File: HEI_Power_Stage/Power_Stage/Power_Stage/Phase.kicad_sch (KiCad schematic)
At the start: 44 parts, among them IC1 AHV85111KNHTR, IC4 AHV85111KNHTR, Q1 EPC2304ENGRT, Q2 EPC2304ENGRT, T1 30k, T2 30k

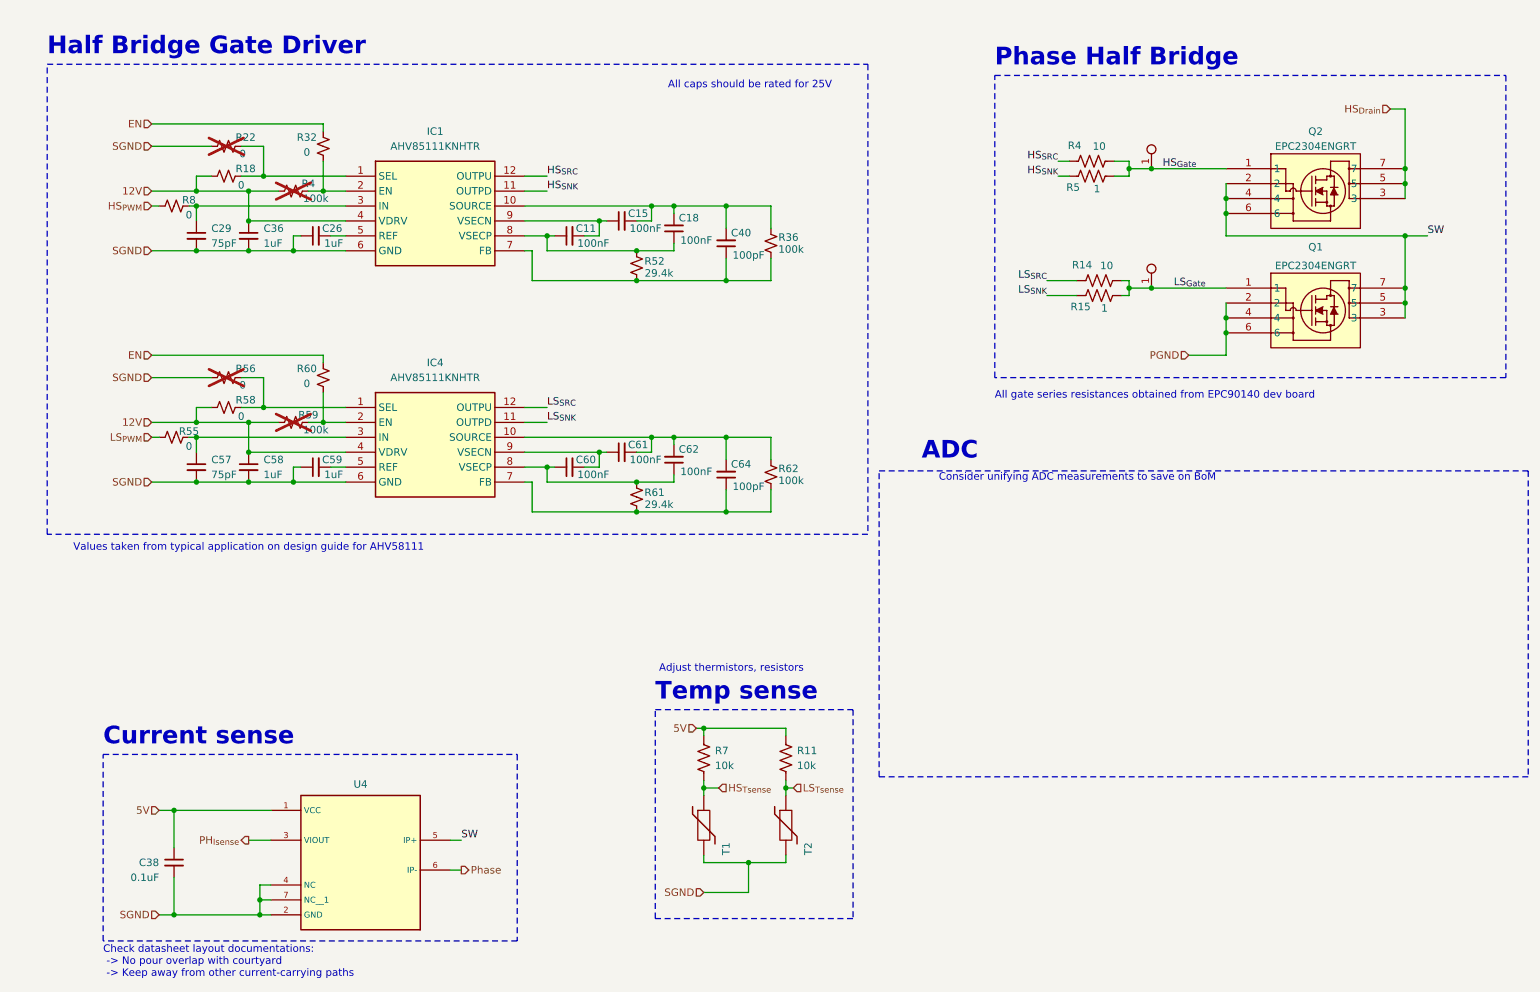
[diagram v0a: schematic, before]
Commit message: new power stage schematic
added iso amp for hv bus sensing
updated connectors
removed isolation page
added notes for new components
need to decide if ADCs go on power or logic board for noise immunity or simpler power stage
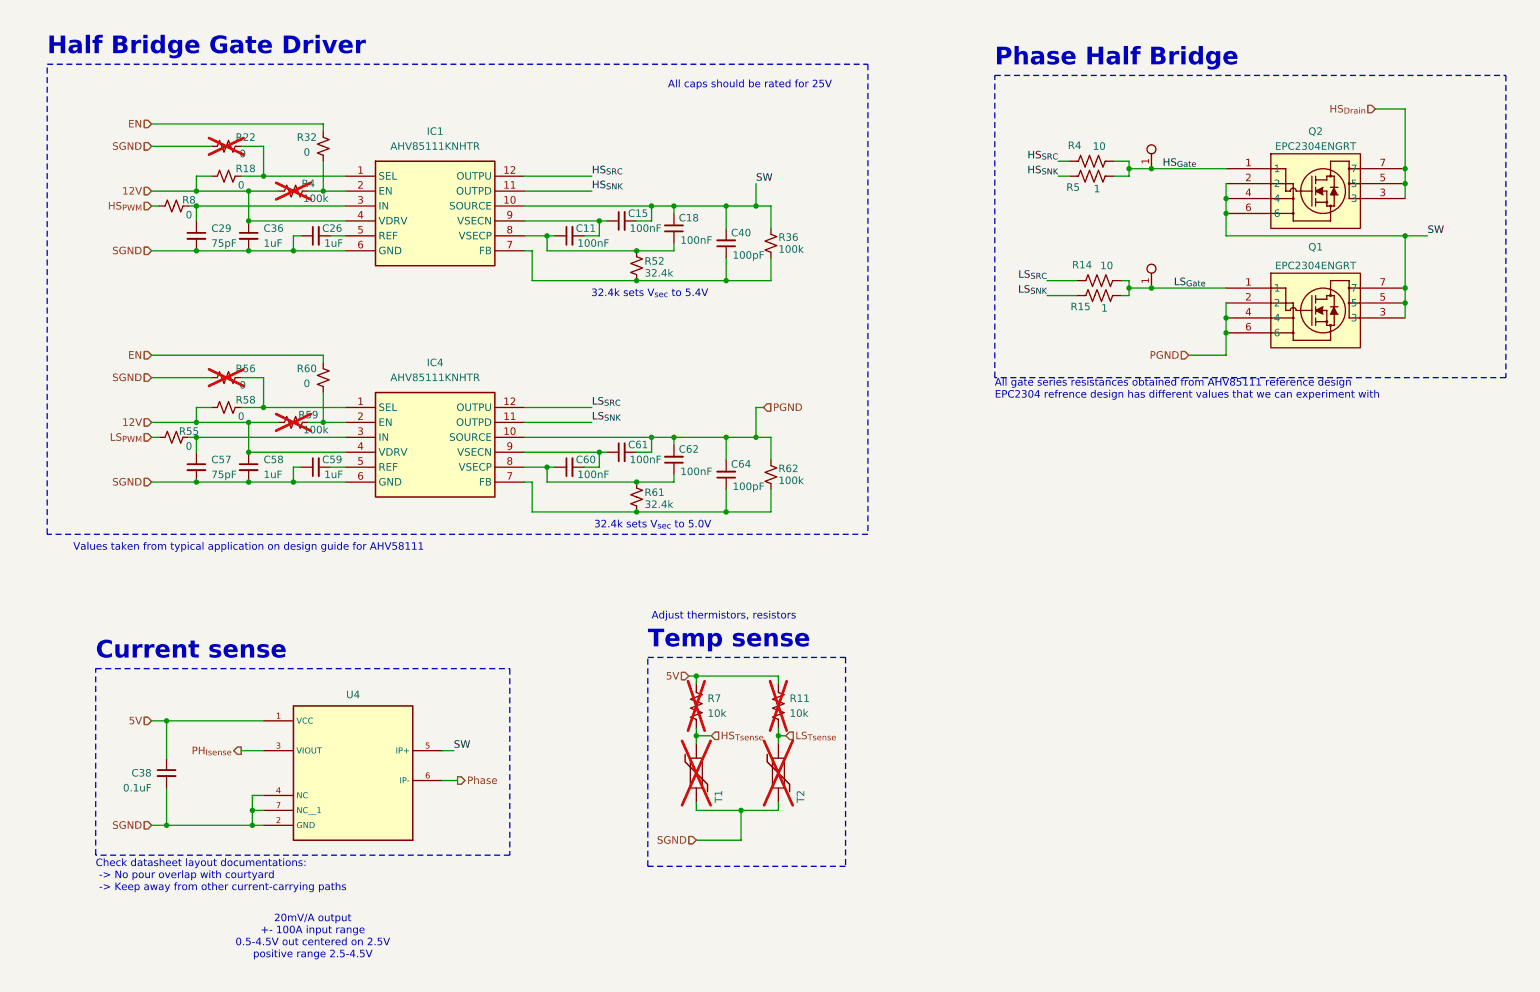
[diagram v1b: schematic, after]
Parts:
- R11, R7, T1, T2: now not fitted
- R52, R61: value 29.4k -> 32.4k
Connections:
- net PGND: now also C61.2, C62.2, C64.2, IC4.10 (SOURCE), R62.1
- net SW: now also C15.2, C18.2, C40.2, IC1.10 (SOURCE), R36.1
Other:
- note added: "20mV/A output +- 100A input range 0.5-4.5V out centered on 2.5V positive range 2.5-4.5V"
- note added: "32.4k sets V_{sec} to 5.0V"
- note added: "32.4k sets V_{sec} to 5.4V"
- note added: "All gate series resistances obtained from AHV85111 reference design EPC2304 refrence design has different values that we can experiment with"
- note removed: "ADC"
- note removed: "All gate series resistances obtained from EPC90140 dev board"
- note removed: "Consider unifying ADC measurements to save on BoM"
- moved on the sheet: C38, U4

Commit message: I think all schematic done
added new mps gate driver, new acs current sense, new differential voltage sense, new 5-5 iso converters.
beginning layout
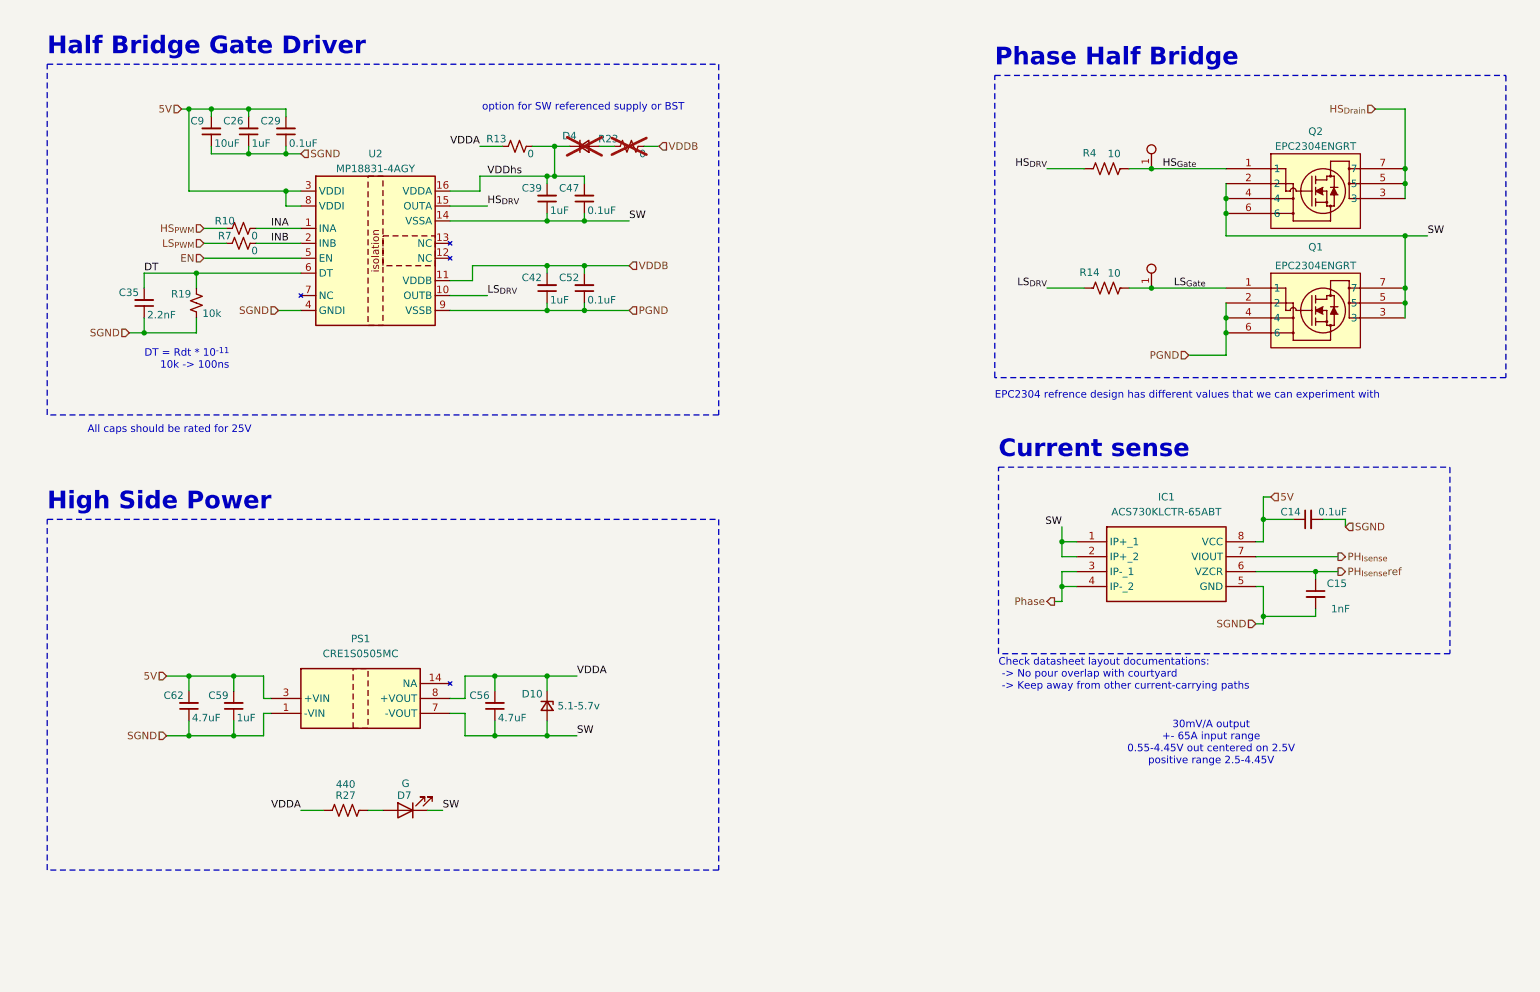
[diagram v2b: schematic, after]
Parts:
- removed C11, C18, C60, C61: 100nF, symbol Device:C_Small
- removed C36, C58: 1uF, symbol Device:C_Small
- removed C38: 0.1uF, Capacitor_SMD:C_0603_1608Metric_Pad1.08x0.95mm_HandSolder, symbol Device:C_Small
- removed C40, C64: 100pF, symbol Device:C_Small
- removed C57: 75pF, symbol Device:C_Small
- removed IC1, IC4: AHV85111KNHTR, AHV85111KNHTR, symbol AHV85111KNHTR:AHV85111KNHTR
- removed R11, R7: 10k, Resistor_SMD:R_0603_1608Metric_Pad0.98x0.95mm_HandSolder, symbol Device:R_US
- removed R15, R5: 1, Resistor_SMD:R_0603_1608Metric_Pad0.98x0.95mm_HandSolder, symbol Device:R_US
- removed R18, R22, R32, R55, R56, R58, R60, R8: 0, symbol Device:R_Small_US
- removed R36, R4, R59, R62: 100k, symbol Device:R_Small_US
- removed R52, R61: 32.4k, symbol Device:R_Small_US
- removed T1, T2: 30k, GTSR_KiCAD_Footprints_SD:2152723803, symbol Device:Thermistor
- removed U4: ~, GTSR_KiCAD_Footprints_SD:XDCR_ACS72981LLRATR-100B5, symbol GTSR_symbol_lib_SD:ACS72981LLRATR-100B5
- added C14, C47, C52: 0.1uF, Capacitor_SMD:C_0603_1608Metric_Pad1.08x0.95mm_HandSolder, symbol Device:C_Small
- added C35: 2.2nF, Capacitor_SMD:C_0603_1608Metric_Pad1.08x0.95mm_HandSolder, symbol Device:C_Small
- added C39, C42: 1uF, Capacitor_SMD:C_0603_1608Metric_Pad1.08x0.95mm_HandSolder, symbol Device:C_Small
- added C56: 4.7uF, Capacitor_SMD:C_0603_1608Metric_Pad1.08x0.95mm_HandSolder, symbol Device:C_Small
- added C9: 10uF, Capacitor_SMD:C_0603_1608Metric_Pad1.08x0.95mm_HandSolder, symbol Device:C_Small
- added D10: 5.1-5.7v, Diode_SMD:D_SOD-128, symbol Device:D_Zener_Small
- added D4: ~, Diode_SMD:D_SOD-523, symbol Device:D_Small
- added D7: G, LED_SMD:LED_0603_1608Metric_Pad1.05x0.95mm_HandSolder, symbol Device:LED
- added IC1: ACS730KLCTR-65ABT, ACS730KLCTR65ABT_KiCad:SOIC127P600X175-8N, symbol ACS730KLCTR-30AB-T:ACS730KLCTR-30AB-T
- added PS1: CRE1S0505MC, CRE1S0505MC_KiCad:CRE1S0505MC, symbol CRE1S0505MC:CRE1S0505MC
- added R10, R13, R7: 0, Resistor_SMD:R_0603_1608Metric_Pad0.98x0.95mm_HandSolder, symbol Device:R_Small_US
- added R19: 10k, Resistor_SMD:R_0603_1608Metric_Pad0.98x0.95mm_HandSolder, symbol Device:R_Small_US
- added R23: 0, LED_SMD:LED_0603_1608Metric_Pad1.05x0.95mm_HandSolder, symbol Device:R_Small_US
- added R27: 440, Resistor_SMD:R_0603_1608Metric_Pad0.98x0.95mm_HandSolder, symbol Device:R_US
- added U2: MP18831-4AGY, Package_SO:SOIC-16W_7.5x10.3mm_P1.27mm, symbol AHV85111KNHTR:MP18831
- C15: value 100nF -> 1nF; footprint (none) -> Capacitor_SMD:C_0603_1608Metric_Pad1.08x0.95mm_HandSolder
- C26, C59: footprint (none) -> Capacitor_SMD:C_0603_1608Metric_Pad1.08x0.95mm_HandSolder
- C29: value 75pF -> 0.1uF; footprint (none) -> Capacitor_SMD:C_0603_1608Metric_Pad1.08x0.95mm_HandSolder
- C62: value 100nF -> 4.7uF; footprint (none) -> Capacitor_SMD:C_0603_1608Metric_Pad1.08x0.95mm_HandSolder
- Q1, Q2: footprint GTSR_KiCAD_Footprints:EPC2304_ECC -> GTSR:EPC2304_ECC
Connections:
- net 5V: now also C26.2, C29.2, C59.2, C62.2, C14.1, C9.2, IC1.8 (VCC), PS1.3 (+VIN), U2.3 (VDDI), U2.8 (VDDI)
- net EN: now also U2.5 (EN)
- net HS_{PWM}: now also R10.1
- net LS_{PWM}: now also R7.1
- net PGND: now also C42.1, C52.1, U2.9 (VSSB); no longer C62.2
- net PH_{Isense}: now also IC1.7 (VIOUT)
- net Phase: now also IC1.3 (IP-_1), IC1.4 (IP-_2)
- net SGND: now also C15.2, C29.1, C62.1, C14.2, C35.1, C9.1, IC1.5 (GND), PS1.1 (-VIN), R19.2, U2.4 (GNDI); no longer C29.2
- net SW: now also C39.1, C47.1, C56.1, D10.2 (A), D7.1 (K), IC1.1 (IP+_1), IC1.2 (IP+_2), PS1.7 (-VOUT), U2.14 (VSSA); no longer C15.2
- net PH_{Isense}ref: now reaches C15.1
- net PH_{Isense}ref: now also IC1.6 (VZCR)
- net HS_{SRC} renamed HS_{DRV}
- net HS_{DRV}: now also U2.15 (OUTA)
- net LS_{SRC} renamed LS_{DRV}
- net LS_{DRV}: now also U2.10 (OUTB)
- new net: D4.2 (A), R23.1
- new net: D7.2 (A), R27.1
- new net DT: C35.2, R19.1, U2.6 (DT)
- new net INA: R10.2, U2.1 (INA)
- new net INB: R7.2, U2.2 (INB)
- new net VDDA: C56.2, D10.1 (K), PS1.8 (+VOUT), R13.1, R27.2
- new net VDDB: C42.2, C52.2, R23.2, U2.11 (VDDB)
- new net VDDhs: C39.2, C47.2, D4.1 (K), R13.2, U2.16 (VDDA)
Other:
- note added: "30mV/A output +- 65A input range 0.55-4.45V out centered on 2.5V positive range 2.5-4.45V"
- note added: "DT = Rdt * 10^{-11} 10k -> 100ns"
- note added: "EPC2304 refrence design has different values that we can experiment with"
- note added: "High Side Power"
- note added: "option for SW referenced supply or BST"
- note removed: "20mV/A output +- 100A input range 0.5-4.5V out centered on 2.5V positive range 2.5-4.5V"
- note removed: "32.4k sets V_{sec} to 5.0V"
- note removed: "32.4k sets V_{sec} to 5.4V"
- note removed: "Adjust thermistors, resistors"
- note removed: "All gate series resistances obtained from AHV85111 reference design EPC2304 refrence design has different values that we can experiment with"
- note removed: "Temp sense"
- note removed: "Values taken from typical application on design guide for AHV58111"
- moved on the sheet: R14, R4

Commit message: more progress
started placement for each half bridge
3d bodies
connectors sorted
options for dc link cap
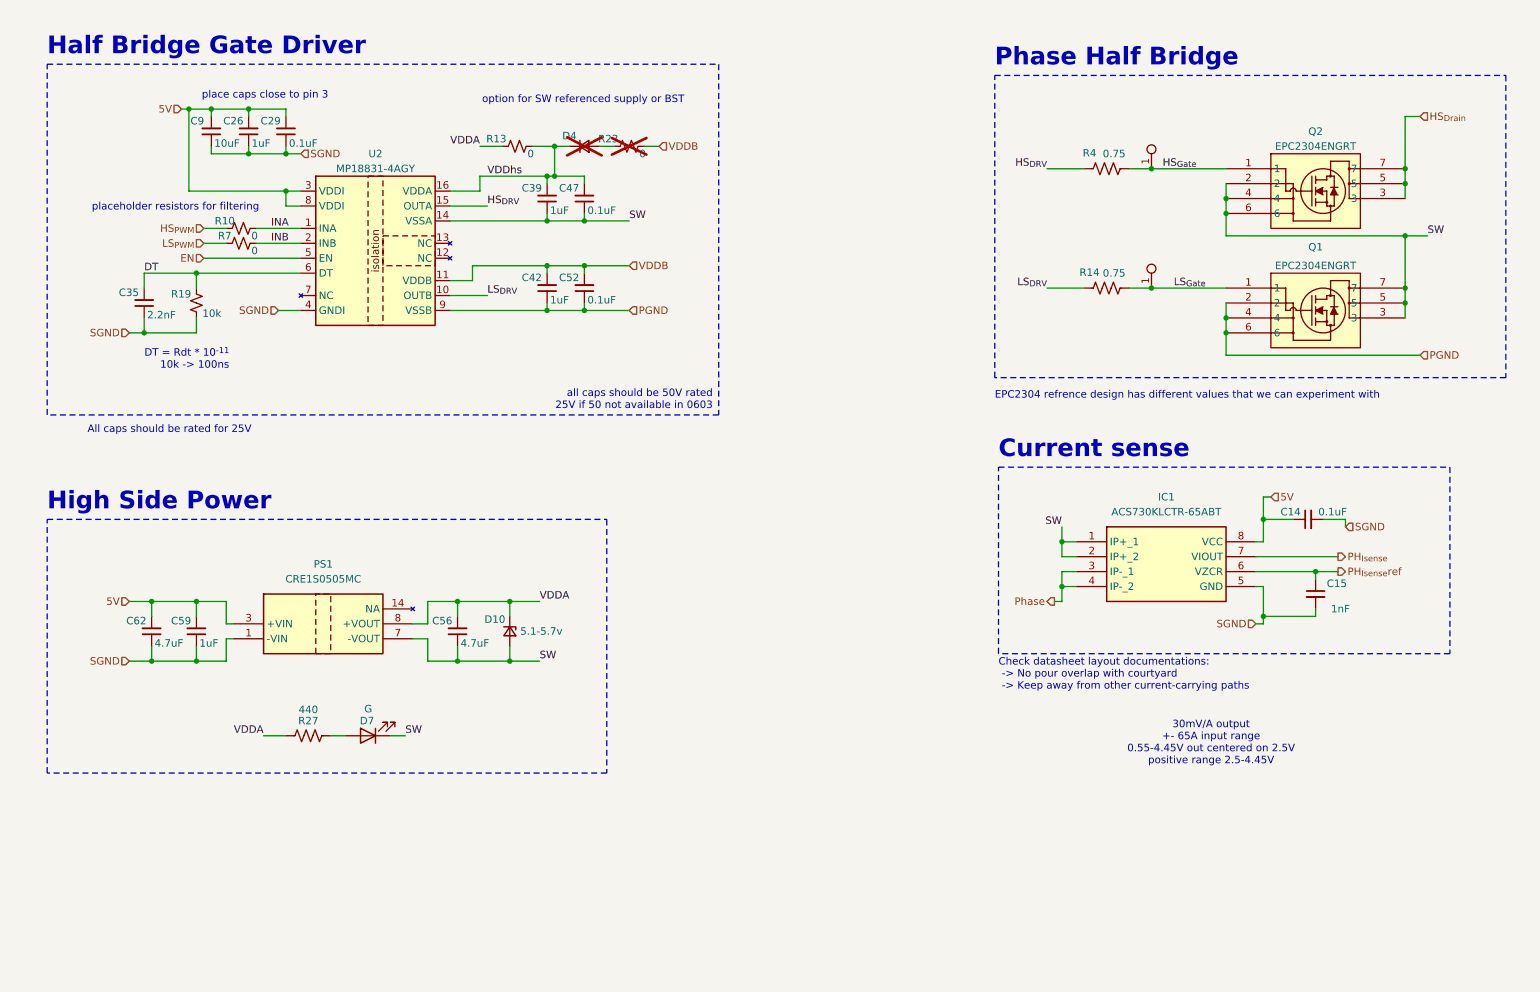
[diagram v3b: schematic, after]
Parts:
- R14, R4: value 10 -> 0.75
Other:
- note added: "all caps should be 50V rated 25V if 50 not available in 0603"
- note added: "place caps close to pin 3"
- note added: "placeholder resistors for filtering"
- moved on the sheet: C56, C59, C62, D10, D7, PS1, R27
